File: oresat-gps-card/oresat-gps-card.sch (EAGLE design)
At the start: 371 parts, among them J1 ORESAT-DEBUG-CONNECTOR-CARD, J100 DM3BT-DSF-PEJS, J102 FTSH-105-XX-X-DV-K, J4 TFM-120-01-L-D-RA, Q1 MMBT2907, Q2 PMV45EN, Q3 DMP2240UDM, Q4 PMV45EN, Q5 MOSFET-PCH-SOT23-6, Q6 MOSFET-PCH-SOT23-6, U1 RCLAMP0504FB, U10 TLVH431, U11 TCAN330, U12 MIC842LYC5, U13 MIC842LYC5, U14 MAX4211FETE, U15 TPS62112, U16 MAX7310ATE, U17 25AAXX, U18 RCLAMP0504FB, U19 BP2G+, U2 TPS2051CDBVR, U20 MAX8510EXK29+T, U21 SF14-1575F5UUA1, U22 LT1719S6, U23 MAX2771ETI+, U24 VENUS838LPX-L, U3 THGBMJG7C2LBAU8, U4 SN74LVC1G07DCK, U5 SKY65723-81, U6 7Q-16.368MBG-T, U7 OSD3358-512M-BSM, U8 MAX8510EXK29+T, U9 MAX8510EXK29+T, Y1 24MHz, Y2 ABS07-32.768KHZ-T

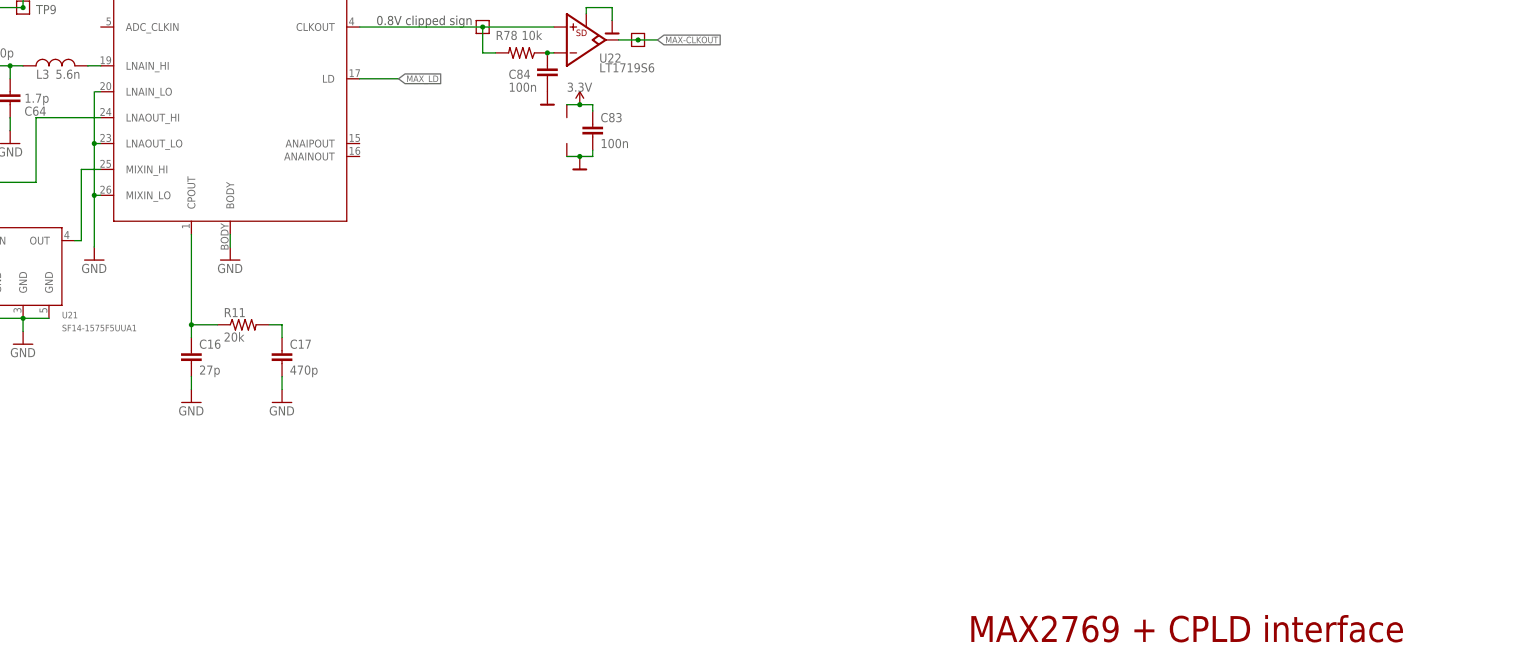
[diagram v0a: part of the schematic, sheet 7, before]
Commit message: OK'd ERC errors.
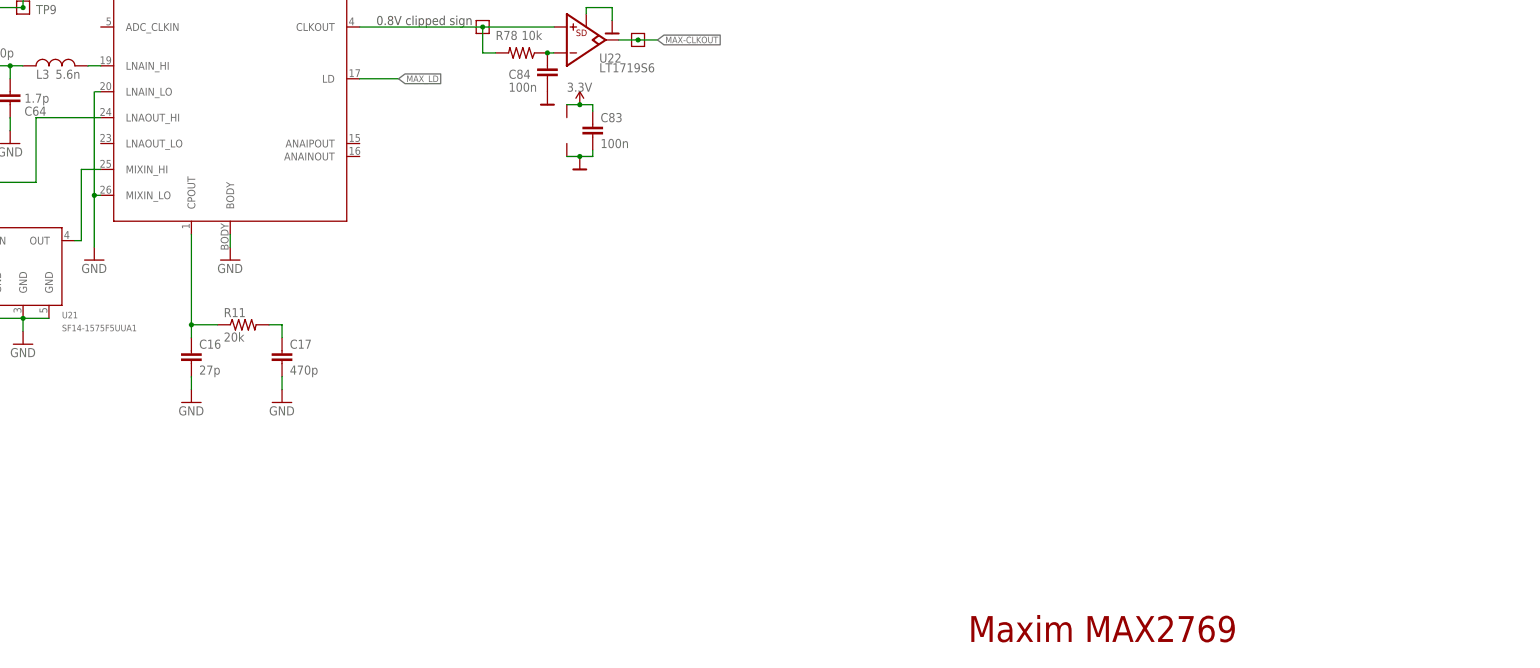
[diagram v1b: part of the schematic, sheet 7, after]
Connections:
- net GND: no longer U23.LNAOUT_LO
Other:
- note added: "Maxim MAX2769"
- note removed: "MAX2769 + CPLD interface"
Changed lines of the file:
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@@
 <?xml version="1.0" encoding="utf-8"?>
 <!DOCTYPE eagle SYSTEM "eagle.dtd">
-<eagle version="9.5.1">
+<eagle version="9.6.1">
 <drawing>
 <settings>
@@
 <wire x1="102.87" y1="162.56" x2="105.41" y2="162.56" width="0.1524" layer="97"/>
 <text x="220.98" y="148.59" size="1.778" layer="97" align="center">0.8V clipped sign</text>
-<text x="327.66" y="26.67" size="5.08" layer="94">MAX2769 + CPLD interface</text>
+<text x="327.66" y="26.67" size="5.08" layer="94">Maxim MAX2769</text>
 </plain>
 <instances>
@@
 <pinref part="U23" gate="G$1" pin="LNAIN_LO"/>
 <wire x1="157.48" y1="134.62" x2="156.21" y2="134.62" width="0.1524" layer="91" style="longdash"/>
-<pinref part="U23" gate="G$1" pin="LNAOUT_LO"/>
-<wire x1="156.21" y1="134.62" x2="156.21" y2="124.46" width="0.1524" layer="91"/>
-<wire x1="156.21" y1="124.46" x2="157.48" y2="124.46" width="0.1524" layer="91"/>
 <pinref part="U23" gate="G$1" pin="MIXIN_LO"/>
-<wire x1="156.21" y1="124.46" x2="156.21" y2="114.3" width="0.1524" layer="91"/>
+<wire x1="156.21" y1="134.62" x2="156.21" y2="114.3" width="0.1524" layer="91"/>
 <wire x1="156.21" y1="114.3" x2="157.48" y2="114.3" width="0.1524" layer="91"/>
-<junction x="156.21" y="124.46"/>
 <wire x1="156.21" y1="114.3" x2="156.21" y2="104.14" width="0.1524" layer="91"/>
 <junction x="156.21" y="114.3"/>
